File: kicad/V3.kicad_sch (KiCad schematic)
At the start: 8 parts

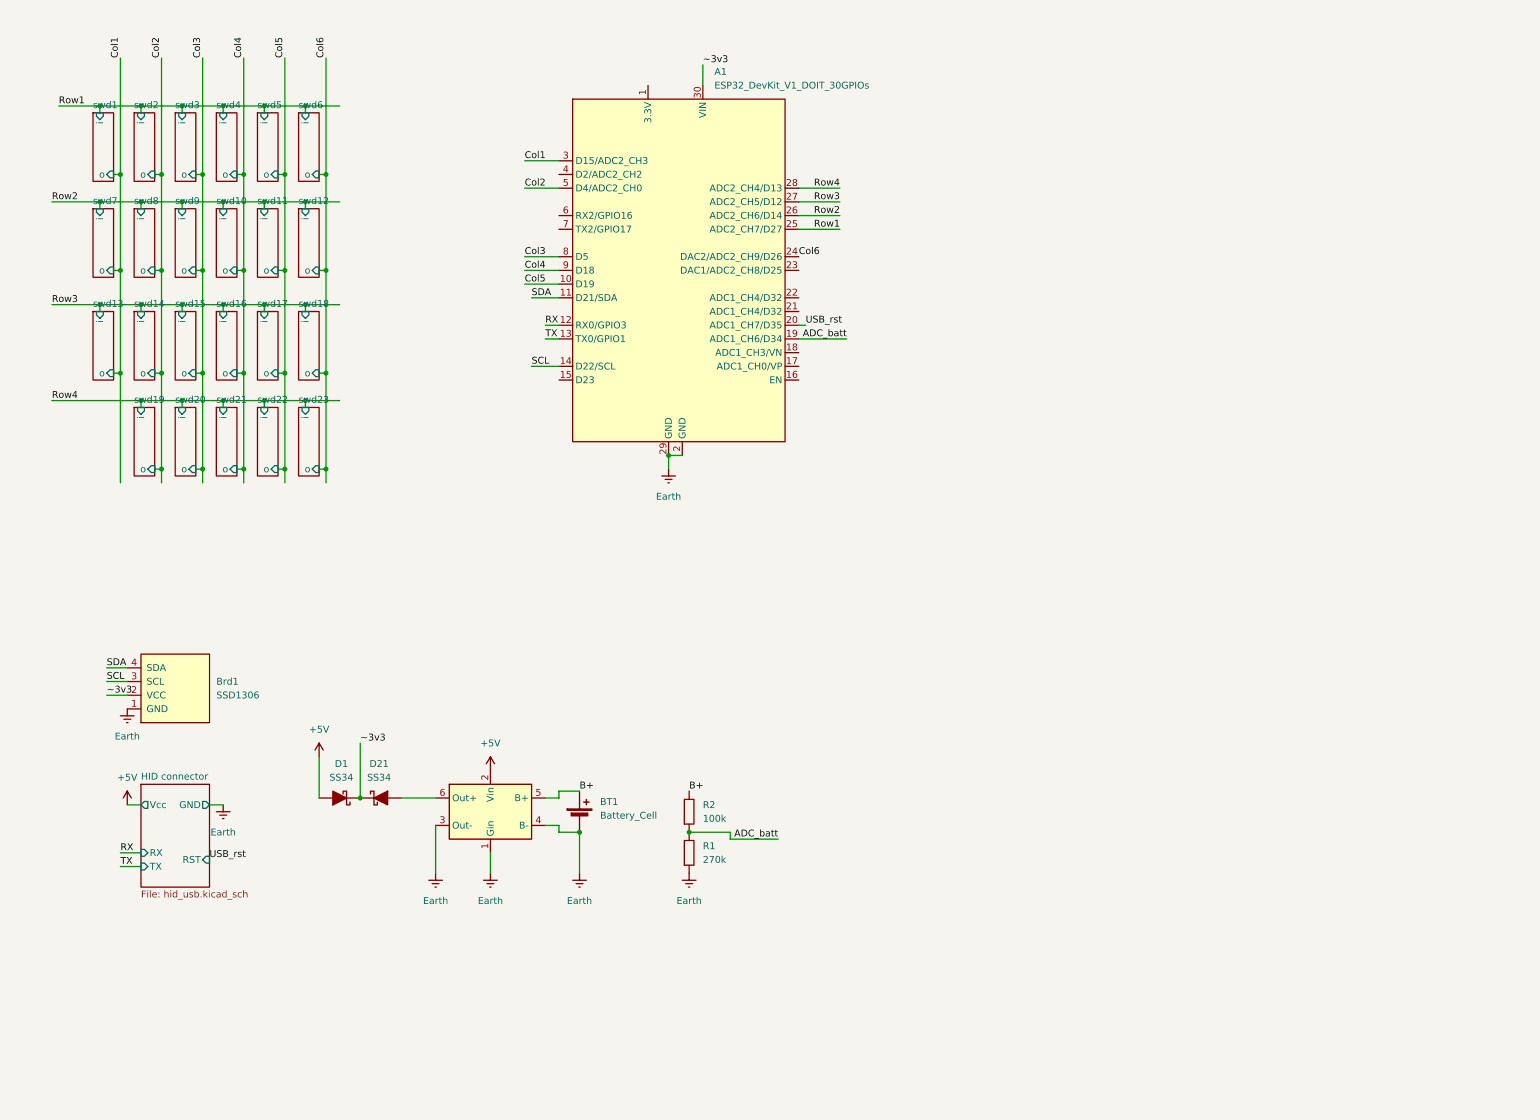
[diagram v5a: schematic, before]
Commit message: switches change
switches no longer use heirarchical schematic
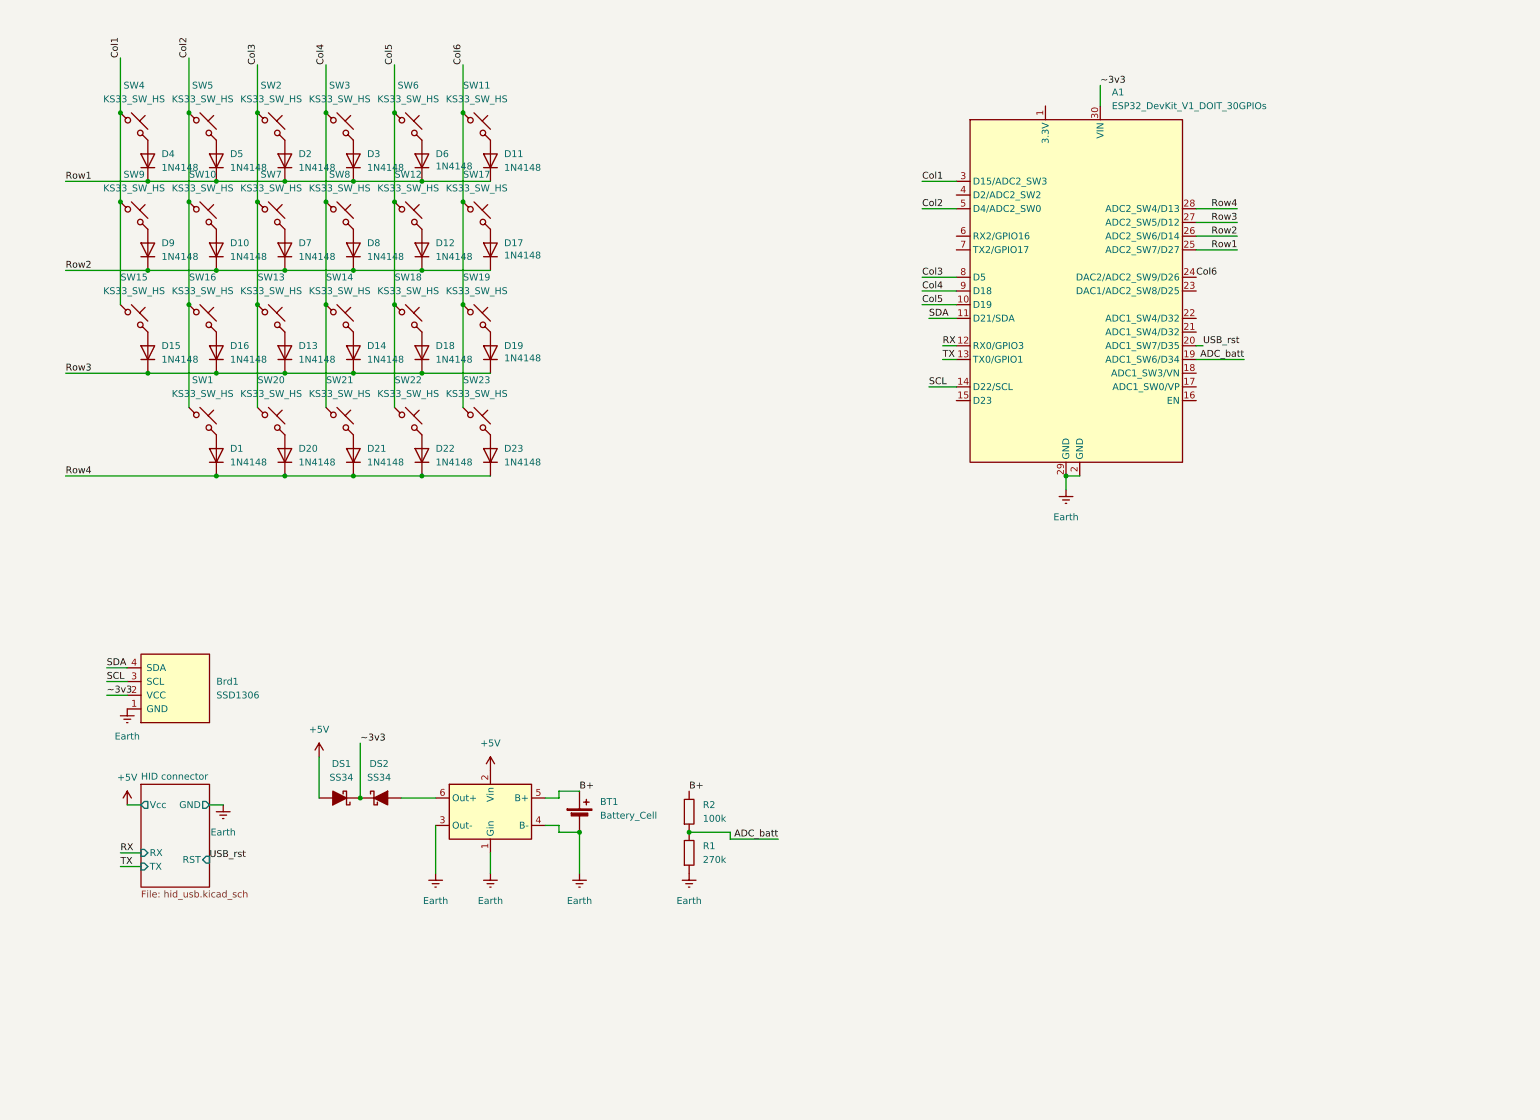
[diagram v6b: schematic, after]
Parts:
- added D1, D10, D11, D12, D13, D14, D15, D16, D17, D18, D19, D2, D20, D21, D22, D23, D3, D4, D5, D6, D7, D8, D9: 1N4148, Diode_THT:D_DO-35_SOD27_P7.62mm_Horizontal, symbol Diode:1N4148
- added SW1, SW10, SW11, SW12, SW13, SW14, SW15, SW16, SW17, SW18, SW19, SW2, SW20, SW21, SW22, SW23, SW3, SW4, SW5, SW6, SW7, SW8, SW9: KS33_SW_HS, keyswitches:Kailh_socket_MX_reversible, symbol PCM_marbastlib-gateron_lp:KS33_SW_HS_KS-2P02B01-02
- U1: footprint Library:HAYATEC TP4056 LIPO CHARGING MODULE -> Library:HAYATEC TP4056 LIPO SWARGING MODULE
- renumbered D1 to DS1, D21 to DS2
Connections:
- net Col1: now also SW15.1, SW4.1, SW9.1
- net Col2: now also SW1.1, SW10.1, SW16.1, SW5.1
- net Col3: now also SW13.1, SW2.1, SW20.1, SW7.1
- net Col4: now also SW14.1, SW21.1, SW3.1, SW8.1
- net Col5: now also SW12.1, SW18.1, SW22.1, SW6.1
- net Col6: now also SW11.1, SW17.1, SW19.1, SW23.1
- net Row1: now also D11.1 (K), D2.1 (K), D3.1 (K), D4.1 (K), D5.1 (K), D6.1 (K)
- net Row2: now also D10.1 (K), D12.1 (K), D17.1 (K), D7.1 (K), D8.1 (K), D9.1 (K)
- net Row3: now also D13.1 (K), D14.1 (K), D15.1 (K), D16.1 (K), D18.1 (K), D19.1 (K)
- net Row4: now also D1.1 (K), D20.1 (K), D21.1 (K), D22.1 (K), D23.1 (K)
- new net: D20.2 (A), SW20.2
- new net: D15.2 (A), SW15.2
- new net: D4.2 (A), SW4.2
- new net: D12.2 (A), SW12.2
- new net: D13.2 (A), SW13.2
- new net: D18.2 (A), SW18.2
- new net: D10.2 (A), SW10.2
- new net: D19.2 (A), SW19.2
- new net: D3.2 (A), SW3.2
- new net: D14.2 (A), SW14.2
- new net: D17.2 (A), SW17.2
- new net: D5.2 (A), SW5.2
- new net: D6.2 (A), SW6.2
- new net: D22.2 (A), SW22.2
- new net: D2.2 (A), SW2.2
- new net: D8.2 (A), SW8.2
- new net: D23.2 (A), SW23.2
- new net: D7.2 (A), SW7.2
- new net: D11.2 (A), SW11.2
- new net: D1.2 (A), SW1.2
- new net: D21.2 (A), SW21.2
- new net: D16.2 (A), SW16.2
- new net: D9.2 (A), SW9.2
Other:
- removed sheet swd1
- removed sheet swd10
- removed sheet swd11
- removed sheet swd12
- removed sheet swd13
- removed sheet swd14
- removed sheet swd15
- removed sheet swd16
- removed sheet swd17
- removed sheet swd18
- removed sheet swd19
- removed sheet swd2
- removed sheet swd20
- removed sheet swd21
- removed sheet swd22
- removed sheet swd23
- removed sheet swd3
- removed sheet swd4
- removed sheet swd5
- removed sheet swd6
- removed sheet swd7
- removed sheet swd8
- removed sheet swd9
- moved on the sheet: A1

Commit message: power
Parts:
- removed Brd1: SSD1306, Library:SSD1306, symbol Librarie:SSD1306
- added U4: SSD1306-128X64-OLED-0.96, Library:SSD1306, symbol Library:SSD1306-128X64-OLED-0.96
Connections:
- net Earth: now also U4.2 (GND)
- net SCL: now also U4.3 (SCL)
- net SDA: now also U4.4 (SDA)
- net +3V3: now reaches A1.1 (3.3V)
- net +3V3: now also U4.1 (VCC)
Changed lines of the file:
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@@
 	(wire
 		(pts
+			(xy 34.29 144.78) (xy 38.1 144.78)
+		)
+		(stroke
+			(width 0)
+			(type default)
+		)
+	)
+	(wire
+		(pts
 			(xy 114.3 158.75) (xy 118.11 158.75)
 		)
@@
 	(wire
 		(pts
-			(xy 30.48 135.89) (xy 34.29 135.89)
+			(xy 34.29 139.7) (xy 38.1 139.7)
 		)
 		(stroke
@@
 	(wire
 		(pts
-			(xy 30.48 140.97) (xy 34.29 140.97)
-		)
-		(stroke
-			(width 0)
-			(type default)
-		)
-	)
-	(wire
-		(pts
 			(xy 50.8 81.28) (xy 63.5 81.28)
 		)
@@
 	(wire
 		(pts
-			(xy 30.48 138.43) (xy 34.29 138.43)
+			(xy 34.29 137.16) (xy 38.1 137.16)
 		)
 		(stroke
@@
 	(wire
 		(pts
+			(xy 34.29 132.08) (xy 38.1 132.08)
+		)
+		(stroke
+			(width 0)
+			(type default)
+		)
+	)
+	(wire
+		(pts
 			(xy 214.63 27.94) (xy 214.63 31.75)
 		)
@@
 	)
 	(label "SDA"
-		(at 30.48 135.89 0)
+		(at 34.29 139.7 0)
 		(effects
 			(font
@@
 		)
 	)
-	(label "~3v3"
-		(at 30.48 140.97 0)
-		(effects
-			(font
-				(size 1.27 1.27)
-			)
-			(justify left bottom)
-		)
-	)
 	(label "Col1"
 		(at 181.61 45.72 0)
@@
 	)
 	(label "SCL"
-		(at 30.48 138.43 0)
+		(at 34.29 137.16 0)
 		(effects
 			(font
@@
 	)
 	(symbol
-		(lib_id "Librarie:SSD1306")
-		(at 43.18 139.7 90)
+		(lib_id "Library:SSD1306-128X64-OLED-0.96")
+		(at 45.72 139.7 0)
 		(unit 1)
 		(exclude_from_sim no)
@@
 		(dnp no)
 		(fields_autoplaced yes)
-		(property "Reference" "Brd1"
-			(at 50.8 138.4299 90)
+		(property "Reference" "U4"
+			(at 57.15 138.4299 0)
 			(effects
 				(font
 					(size 1.27 1.27)
 				)
-				(justify right)
+				(justify left)
 			)
 		)
-		(property "Value" "SSD1306"
-			(at 50.8 140.9699 90)
+		(property "Value" "SSD1306-128X64-OLED-0.96"
+			(at 49.022 150.622 0)
 			(effects
 				(font
 					(size 1.27 1.27)
 				)
-				(justify right)
+				(hide yes)
 			)
 		)
 		(property "Footprint" "Library:SSD1306"
-			(at 36.83 139.7 0)
+			(at 47.752 127.508 0)
 			(effects
 				(font
@@
 		)
 		(property "Datasheet" ""
-			(at 36.83 139.7 0)
+			(at 45.72 139.7 0)
 			(effects
 				(font
@@
 			)
 		)
-		(property "Description" "SSD1306 OLED"
-			(at 43.18 139.7 0)
+		(property "Description" ""
+			(at 45.72 139.7 0)
 			(effects
 				(font
@@
 			)
 		)
-		(pin "3"
+		(pin "2"
 		)
 		(pin "1"
 		)
-		(pin "2"
+		(pin "3"
 		)
 		(pin "4"
@@
 			(project ""
 				(path "/55ac274f-6d39-4edb-ae03-cf051723ec39"
-					(reference "Brd1")
+					(reference "U4")
 					(unit 1)
 				)
@@
 	)
 	(symbol
+		(lib_id "power:+3V3")
+		(at 204.47 31.75 0)
+		(unit 1)
+		(exclude_from_sim no)
+		(in_bom yes)
+		(on_board yes)
+		(dnp no)
+		(fields_autoplaced yes)
+		(property "Reference" "#PWR011"
+			(at 204.47 35.56 0)
+			(effects
+				(font
+					(size 1.27 1.27)
+				)
+				(hide yes)
+			)
+		)
+		(property "Value" "+3V3"
+			(at 204.47 26.67 0)
+			(effects
+				(font
+					(size 1.27 1.27)
+				)
+			)
+		)
+		(property "Footprint" ""
+			(at 204.47 31.75 0)
+			(effects
+				(font
+					(size 1.27 1.27)
+				)
+				(hide yes)
+			)
+		)
+		(property "Datasheet" ""
+			(at 204.47 31.75 0)
+			(effects
+				(font
+					(size 1.27 1.27)
+				)
+				(hide yes)
+			)
+		)
+		(property "Description" "Power symbol creates a global label with name \"+3V3\""
+			(at 204.47 31.75 0)
+			(effects
+				(font
+					(size 1.27 1.27)
+				)
+				(hide yes)
+			)
+		)
+		(pin "1"
+		)
+		(instances
+			(project ""
+				(path "/55ac274f-6d39-4edb-ae03-cf051723ec39"
+					(reference "#PWR011")
+					(unit 1)
+				)
+			)
+		)
+	)
+	(symbol
 		(lib_id "Device:Battery_Cell")
 		(at 118.11 163.83 0)
@@
 	(symbol
 		(lib_id "power:Earth")
-		(at 34.29 143.51 0)
+		(at 34.29 144.78 0)
 		(unit 1)
 		(exclude_from_sim no)
@@
 		(dnp no)
 		(property "Reference" "#PWR02"
-			(at 34.29 149.86 0)
+			(at 34.29 151.13 0)
 			(effects
 				(font
@@
 		)
 		(property "Value" "Earth"
-			(at 34.29 148.59 0)
+			(at 34.29 149.86 0)
 			(effects
 				(font
@@
 		)
 		(property "Footprint" ""
-			(at 34.29 143.51 0)
+			(at 34.29 144.78 0)
 			(effects
 				(font
@@
 		)
 		(property "Datasheet" "~"
-			(at 34.29 143.51 0)
+			(at 34.29 144.78 0)
 			(effects
 				(font
@@
 		)
 		(property "Description" "Power symbol creates a global label with name \"Earth\""
-			(at 34.29 143.51 0)
+			(at 34.29 144.78 0)
 			(effects
 				(font
@@
 					(unit 1)
 				)
+			)
+		)
+	)
+	(symbol
+		(lib_id "power:+3V3")
+		(at 34.29 132.08 0)
+		(unit 1)
+		(exclude_from_sim no)
+		(in_bom yes)
+		(on_board yes)
+		(dnp no)
+		(fields_autoplaced yes)
+		(property "Reference" "#PWR012"
+			(at 34.29 135.89 0)
+			(effects
+				(font
+					(size 1.27 1.27)
+				)
+				(hide yes)
+			)
+		)
+		(property "Value" "+3V3"
+			(at 34.29 127 0)
+			(effects
+				(font
+					(size 1.27 1.27)
+				)
+			)
+		)
+		(property "Footprint" ""
+			(at 34.29 132.08 0)
+			(effects
+				(font
+					(size 1.27 1.27)
+				)
+				(hide yes)
+			)
+		)
+		(property "Datasheet" ""
+			(at 34.29 132.08 0)
+			(effects
+				(font
+					(size 1.27 1.27)
+				)
+				(hide yes)
+			)
+		)
+		(property "Description" "Power symbol creates a global label with name \"+3V3\""
+			(at 34.29 132.08 0)
+			(effects
+				(font
+					(size 1.27 1.27)
+				)
+				(hide yes)
+			)
+		)
+		(pin "1"
+		)
+		(instances
+			(project "V3"
+				(path "/55ac274f-6d39-4edb-ae03-cf051723ec39"
+					(reference "#PWR012")
+					(unit 1)
+				)

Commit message: working version
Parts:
- removed A1: ESP32_DevKit_V1_DOIT_30GPIOs, PCM_SL_Development_Boards:DOIT_ESP32_DEVKIT_30Pins, symbol PCM_SL_Development_Board:ESP32_DevKit_V1_DOIT_30GPIOs
- removed D22, D23: 1N4148, Diode_THT:D_DO-35_SOD27_P7.62mm_Horizontal, symbol Diode:1N4148
- removed DS1, DS2: SS34, PCM_Diode_SMD_AKL:D_SMC, symbol PCM_Diode_Schottky_AKL:SS34
- removed R1: 270k, Resistor_THT:R_Axial_DIN0207_L6.3mm_D2.5mm_P10.16mm_Horizontal, symbol PCM_SL_Resistors:270k
- removed R2: 100k, Resistor_THT:R_Axial_DIN0207_L6.3mm_D2.5mm_P10.16mm_Horizontal, symbol PCM_SL_Resistors:100k
- removed SW23: KS33_SW_HS, keyswitches:Kailh_socket_MX_reversible, symbol PCM_marbastlib-gateron_lp:KS33_SW_HS_KS-2P02B01-02
- removed U1: ~, Library:HAYATEC TP4056 LIPO SWARGING MODULE, symbol Library:TP4056_usb_module
- added D22: 1N4148, PCM_Diode_THT_AKL:D_DO-35_SOD27_P7.62mm_Horizontal, symbol PCM_Diode_AKL:1N4148
- added SW23: Slide_Switch_SPDT_P3mm_10x5x10mm, PCM_SL_Devices:Slide_Switch_SPDT_P3mm_10x5x10mm, symbol PCM_SL_Devices:Slide_Switch_SPDT_P3mm_10x5x10mm
- added U1: SuperMini nRF52840, PCM_marbastlib-xp-promicroish:SuperMini_nRF52840_AH_USBup, symbol PCM_marbastlib-promicroish:SuperMini_nRF52840
- D1, D10, D11, D12, D13, D14, D15, D16, D17, D18, D19, D2, D20, D21, D3, D4, D5, D6, D7, D8, D9: footprint Diode_THT:D_DO-35_SOD27_P7.62mm_Horizontal -> PCM_Diode_THT_AKL:D_DO-35_SOD27_P7.62mm_Horizontal; symbol Diode:1N4148 -> PCM_Diode_AKL:1N4148
- SW1, SW10, SW11, SW12, SW13, SW14, SW15, SW16, SW17, SW18, SW19, SW2, SW20, SW21, SW22, SW3, SW4, SW5, SW6, SW7, SW8, SW9: footprint keyswitches:Kailh_socket_MX_reversible -> keyswitches:Kailh_socket_PG1350_reversible
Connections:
- net +3V3: now also U1.16 (3V3)
- net B+: now also SW23.3, U1.13 (BAT+), U1.29 (BAT+); no longer BT1.1 (+)
- net Col1: now also SW13.1, SW18.1, SW7.1, U1.10 (P0.11); no longer SW15.1, SW4.1, SW9.1
- net Col2: now also SW11.1, SW17.1, U1.11 (P1.04-LF); no longer SW1.1, SW10.1, SW16.1
- net Col3: now also SW15.1, SW19.1, SW3.1, SW9.1, U1.12 (P1.06-LF); no longer SW13.1, SW2.1, SW20.1, SW7.1
- net Col4: now also SW1.1, SW12.1, SW20.1, SW6.1, U1.20 (P1.15-LF); no longer SW14.1, SW21.1, SW3.1, SW8.1
- net Col5: now also SW14.1, SW2.1, SW21.1, SW8.1, U1.19 (P0.02-LF); no longer SW12.1, SW18.1, SW22.1, SW6.1
- net Col6: now also SW10.1, SW16.1, SW22.1, SW4.1, U1.18 (P0.29-LF); no longer SW11.1, SW17.1, SW19.1
- net Earth: now also U1.14 (GND), U1.28 (GND), U1.3 (GND), U1.4 (GND)
- net Row1: now also D1.1 (K), D7.1 (K), U1.24 (P0.09-LF); no longer D11.1 (K), D6.1 (K)
- net Row2: now also D11.1 (K), D13.1 (K), D6.1 (K), U1.23 (P0.10-LF); no longer D12.1 (K), D17.1 (K), D7.1 (K)
- net Row3: now also D12.1 (K), D17.1 (K), U1.22 (P1.11-LF); no longer D13.1 (K), D19.1 (K)
- net Row4: now also D19.1 (K), D22.1 (K), U1.21 (P1.13-LF); no longer D1.1 (K)
- net SCL: now also U1.6 (P0.20)
- net SDA: now also U1.5 (P0.17)
- net at SW22.2: now also D22.2 (A)
- new net: BT1.1 (+), SW23.1
- no-connect marks 0 -> 1
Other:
- removed sheet HID connector
- moved on the sheet: SW1, SW10, SW11, SW12, SW13, SW14, SW15, SW16, SW17, SW18, SW19, SW2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
